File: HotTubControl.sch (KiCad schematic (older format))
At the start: 27 parts, among them J1 Wasser Vorlauf, J2 Wasser Rücklauf, J3 Massagepumpe, J4 Filterpumpe, J5 Füllstandsensor, J6 Conn_01x03, K1 JV-KT, Q1 BC337, Q2 BSS138

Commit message: neue 3d Elemente
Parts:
- B1: symbol LoraClient-eagle-import:WEMOS-D1-MINI -> HotTubControl-rescue:WEMOS-D1-MINI-LoraClient-eagle-import
- C2: symbol LoraClient-eagle-import:CPOL-EU085CS-1AR -> Device:CP
- K1: symbol LoraClient-eagle-import:JV-KT -> HotTubControl-rescue:JV-KT-LoraClient-eagle-import
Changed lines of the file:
@@
 $EndComp
 $Comp
-L LoraClient-eagle-import:JV-KT K1
+L HotTubControl-rescue:JV-KT-LoraClient-eagle-import K1
 U 1 1 61660A14
 P 3700 4950
@@
 	1950 3950 2000 3950
 $Comp
-L LoraClient-eagle-import:JV-KT K1
+L HotTubControl-rescue:JV-KT-LoraClient-eagle-import K1
 U 2 1 6166404C
 P 1750 3750
@@
 Connection ~ 1650 5300
 $Comp
-L LoraClient-eagle-import:WEMOS-D1-MINI B1
+L HotTubControl-rescue:WEMOS-D1-MINI-LoraClient-eagle-import B1
 U 1 1 616A05F9
 P 5750 3700
@@
 	9300 4750 8400 4750
 $Comp
-L LoraClient-eagle-import:CPOL-EU085CS-1AR C2
+L Device:CP C2
 U 1 1 61684BD0
 P 1800 5100

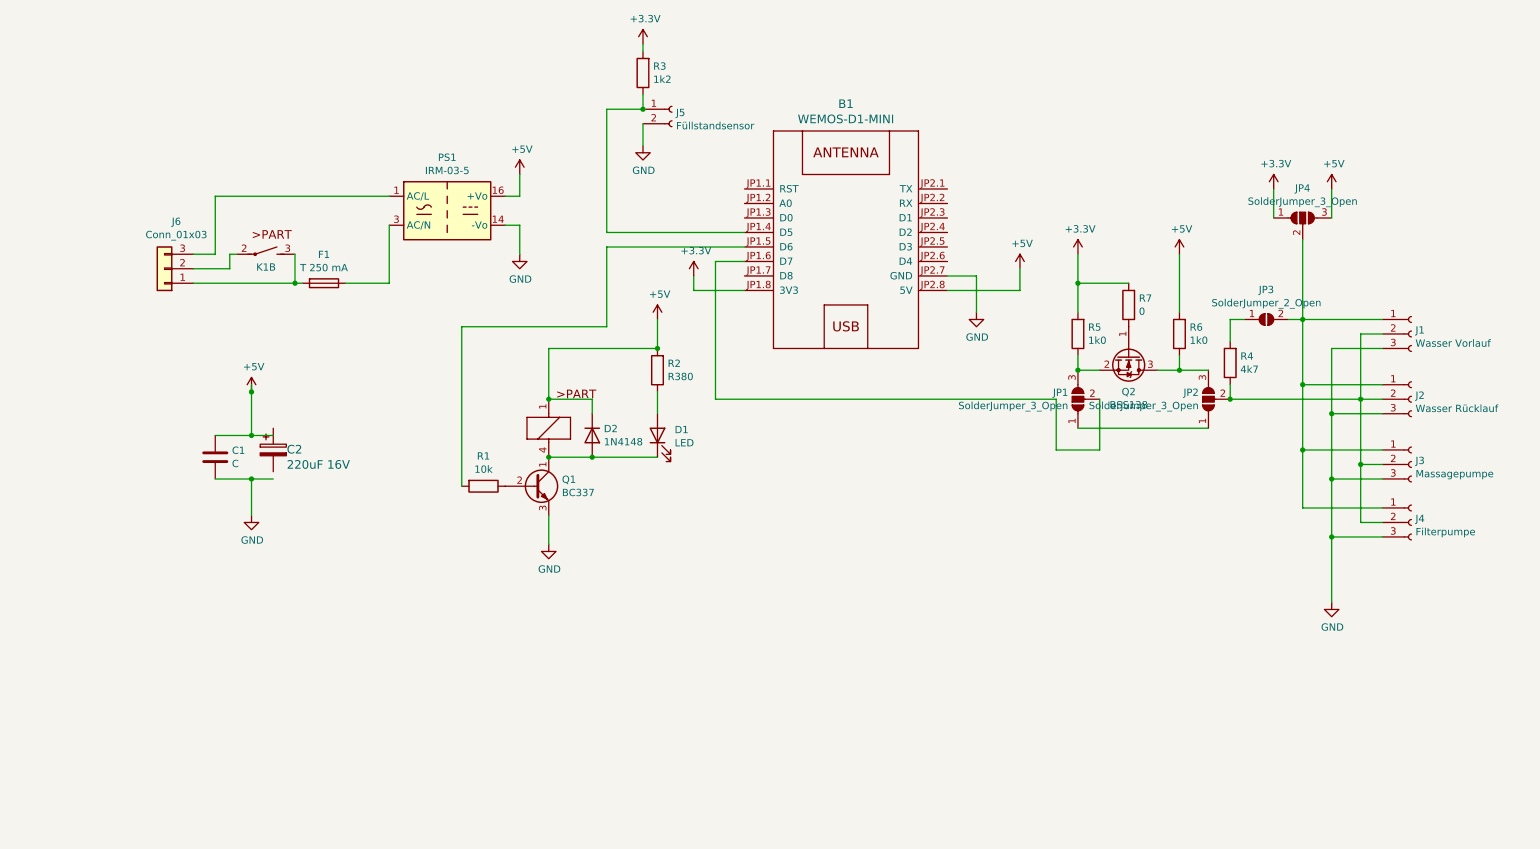
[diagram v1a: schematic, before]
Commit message: V2.0 added one channesl
Ein zweiter Relaiskanal zu Steuerung der  Massagepumpe wurde integriert
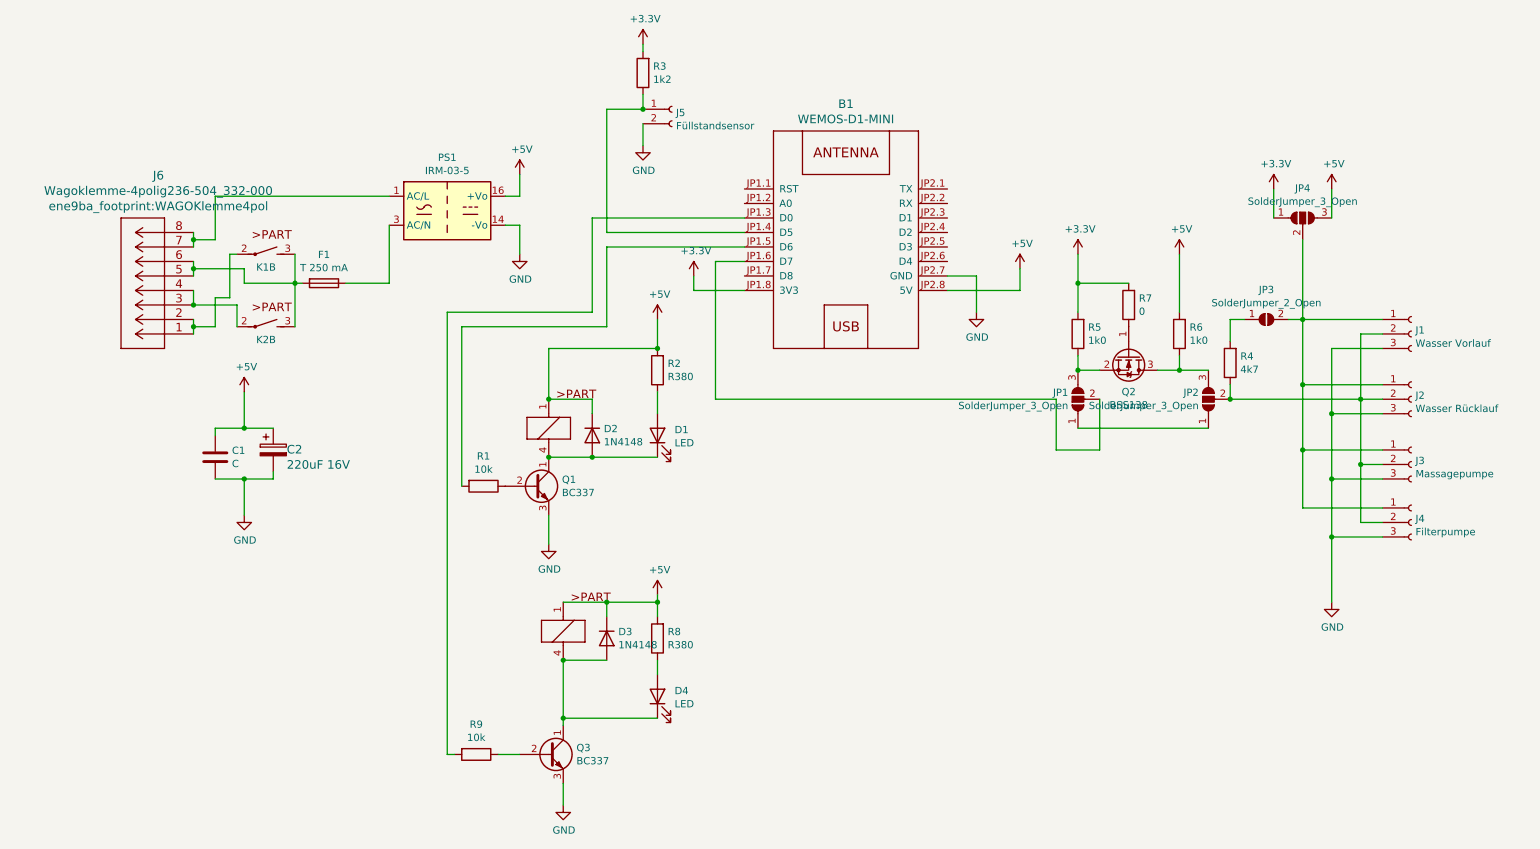
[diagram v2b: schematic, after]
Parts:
- removed J6: Conn_01x03, ene9ba_footprint:236-503, symbol Connector_Generic:Conn_01x03
- added D3: 1N4148, Diode_THT:D_DO-35_SOD27_P7.62mm_Horizontal, symbol Diode:1N4148
- added D4: LED, LED_THT:LED_D5.0mm, symbol Device:LED
- added J6: Wagoklemme-4polig236-504_332-000, ene9ba_footprint:WAGOKlemme4pol, symbol HotTubControl-rescue:Wagoklemme-4polig236-504_332-000-ene9ba_library
- added K2: JV-KT, SamacSys_Parts:JV24SKT, symbol HotTubControl-rescue:JV-KT-LoraClient-eagle-import
- added Q3: BC337, Package_TO_SOT_THT:TO-92_Inline, symbol Transistor_BJT:BC337
- added R8: R380, Resistor_THT:R_Axial_DIN0207_L6.3mm_D2.5mm_P15.24mm_Horizontal, symbol Device:R
- added R9: 10k, Resistor_THT:R_Axial_DIN0207_L6.3mm_D2.5mm_P15.24mm_Horizontal, symbol Device:R
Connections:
- wire segments 93 -> 125
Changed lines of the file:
@@
 L power:GND #PWR0104
 U 1 1 6169E8F8
-P 1650 5550
-F 0 "#PWR0104" H 1650 5300 50  0001 C CNN
-F 1 "GND" H 1655 5377 50  0000 C CNN
-F 2 "" H 1650 5550 50  0001 C CNN
-F 3 "" H 1650 5550 50  0001 C CNN
-	1    1650 5550
-	1    0    0    -1
-$EndComp
-Wire Wire Line
-	1400 5000 1650 5000
-Wire Wire Line
-	1650 5000 1650 4700
-Connection ~ 1650 5000
-Wire Wire Line
-	1650 5000 1800 5000
-Wire Wire Line
-	1650 5550 1650 5300
-Wire Wire Line
-	1400 5300 1650 5300
-Wire Wire Line
-	1650 5300 1800 5300
-Connection ~ 1650 5300
+P 1600 5550
+F 0 "#PWR0104" H 1600 5300 50  0001 C CNN
+F 1 "GND" H 1605 5377 50  0000 C CNN
+F 2 "" H 1600 5550 50  0001 C CNN
+F 3 "" H 1600 5550 50  0001 C CNN
+	1    1600 5550
+	1    0    0    -1
+$EndComp
 $Comp
 L HotTubControl-rescue:WEMOS-D1-MINI-LoraClient-eagle-import B1
@@
 L power:+5V #PWR0112
 U 1 1 61734FF9
-P 1650 4700
-F 0 "#PWR0112" H 1650 4550 50  0001 C CNN
-F 1 "+5V" H 1665 4873 50  0000 C CNN
-F 2 "" H 1650 4700 50  0001 C CNN
-F 3 "" H 1650 4700 50  0001 C CNN
-	1    1650 4700
-	1    0    0    -1
-$EndComp
-Connection ~ 1650 4700
-Wire Wire Line
-	1650 4700 1650 4650
+P 1600 4700
+F 0 "#PWR0112" H 1600 4550 50  0001 C CNN
+F 1 "+5V" H 1615 4873 50  0000 C CNN
+F 2 "" H 1600 4700 50  0001 C CNN
+F 3 "" H 1600 4700 50  0001 C CNN
+	1    1600 4700
+	1    0    0    -1
+$EndComp
 $Comp
 L power:+3.3V #PWR0113
@@
 	1    0    0    -1
 $EndComp
-$Comp
-L Connector_Generic:Conn_01x03 J6
-U 1 1 617860F2
-P 1050 3850
-F 0 "J6" H 968 3525 50  0000 C CNN
-F 1 "Conn_01x03" H 968 3616 50  0000 C CNN
-F 2 "ene9ba_footprint:236-503" H 1050 3850 50  0001 C CNN
-F 3 "~" H 1050 3850 50  0001 C CNN
-	1    1050 3850
-	-1   0    0    1
-$EndComp
-Wire Wire Line
-	1250 3950 1950 3950
 Connection ~ 1950 3950
 Wire Wire Line
 	1550 3750 1500 3750
-Wire Wire Line
-	1500 3750 1500 3850
-Wire Wire Line
-	1500 3850 1250 3850
-Wire Wire Line
-	1250 3750 1400 3750
-Wire Wire Line
-	1400 3750 1400 3350
 Wire Wire Line
 	1400 3350 2600 3350
@@
 Wire Wire Line
 	7350 3950 7350 4150
+$Comp
+L power:+5V #PWR0117
+U 1 1 618D82FF
+P 4450 6100
+F 0 "#PWR0117" H 4450 5950 50  0001 C CNN
+F 1 "+5V" H 4465 6273 50  0000 C CNN
+F 2 "" H 4450 6100 50  0001 C CNN
+F 3 "" H 4450 6100 50  0001 C CNN
+	1    4450 6100
+	1    0    0    -1
+$EndComp
+$Comp
+L Device:R R8
+U 1 1 618D957A
+P 4450 6400
+F 0 "R8" H 4380 6354 50  0000 R CNN
+F 1 "R380" H 4380 6445 50  0000 R CNN
+F 2 "Resistor_THT:R_Axial_DIN0207_L6.3mm_D2.5mm_P15.24mm_Horizontal" V 4380 6400 50  0001 C CNN
+F 3 "~" H 4450 6400 50  0001 C CNN
+	1    4450 6400
+	-1   0    0    1
+$EndComp
+$Comp
+L HotTubControl-rescue:JV-KT-LoraClient-eagle-import K2
+U 1 1 618DA08B
+P 3800 6350
+F 0 "K2" H 3800 6350 50  0001 C CNN
+F 1 "JV-KT" H 3850 6465 59  0001 L BNN
+F 2 "SamacSys_Parts:JV24SKT" H 3800 6350 50  0001 C CNN
+F 3 "" H 3800 6350 50  0001 C CNN
+	1    3800 6350
+	1    0    0    -1
+$EndComp
+$Comp
+L Diode:1N4148 D3
+U 1 1 618DD5D3
+P 4100 6400
+F 0 "D3" V 4054 6480 50  0000 L CNN
+F 1 "1N4148" V 4145 6480 50  0000 L CNN
+F 2 "Diode_THT:D_DO-35_SOD27_P7.62mm_Horizontal" H 4100 6225 50  0001 C CNN
+F 3 "https://assets.nexperia.com/documents/data-sheet/1N4148_1N4448.pdf" H 4100 6400 50  0001 C CNN
+	1    4100 6400
+	0    1    1    0
+$EndComp
+$Comp
+L Device:LED D4
+U 1 1 618DED1E
+P 4450 6800
+F 0 "D4" V 4489 6682 50  0000 R CNN
+F 1 "LED" V 4398 6682 50  0000 R CNN
+F 2 "LED_THT:LED_D5.0mm" H 4450 6800 50  0001 C CNN
+F 3 "~" H 4450 6800 50  0001 C CNN
+	1    4450 6800
+	0    -1   -1   0
+$EndComp
+$Comp
+L Transistor_BJT:BC337 Q3
+U 1 1 618DF9A8
+P 3700 7200
+F 0 "Q3" H 3891 7246 50  0000 L CNN
+F 1 "BC337" H 3891 7155 50  0000 L CNN
+F 2 "Package_TO_SOT_THT:TO-92_Inline" H 3900 7125 50  0001 L CIN
+F 3 "https://diotec.com/tl_files/diotec/files/pdf/datasheets/bc337.pdf" H 3700 7200 50  0001 L CNN
+	1    3700 7200
+	1    0    0    -1
+$EndComp
+$Comp
+L Device:R R9
+U 1 1 618E161A
+P 3200 7200
+F 0 "R9" V 2993 7200 50  0000 C CNN
+F 1 "10k" V 3084 7200 50  0000 C CNN
+F 2 "Resistor_THT:R_Axial_DIN0207_L6.3mm_D2.5mm_P15.24mm_Horizontal" V 3130 7200 50  0001 C CNN
+F 3 "~" H 3200 7200 50  0001 C CNN
+	1    3200 7200
+	0    1    1    0
+$EndComp
+$Comp
+L power:GND #PWR0118
+U 1 1 618E1F2A
+P 3800 7550
+F 0 "#PWR0118" H 3800 7300 50  0001 C CNN
+F 1 "GND" H 3805 7377 50  0000 C CNN
+F 2 "" H 3800 7550 50  0001 C CNN
+F 3 "" H 3800 7550 50  0001 C CNN
+	1    3800 7550
+	1    0    0    -1
+$EndComp
+Wire Wire Line
+	4450 6100 4450 6150
+Wire Wire Line
+	4450 6550 4450 6650
+Wire Wire Line
+	4450 6950 3800 6950
+Wire Wire Line
+	3800 6950 3800 7000
+Wire Wire Line
+	4100 6550 3800 6550
+Wire Wire Line
+	4100 6250 4100 6150
+Wire Wire Line
+	4100 6150 3800 6150
+Wire Wire Line
+	4100 6150 4450 6150
+Connection ~ 4100 6150
+Connection ~ 4450 6150
+Wire Wire Line
+	4450 6150 4450 6250
+Wire Wire Line
+	3800 6550 3800 6950
+Connection ~ 3800 6550
+Connection ~ 3800 6950
+Wire Wire Line
+	3500 7200 3350 7200
+Wire Wire Line
+	5050 3500 4000 3500
+Wire Wire Line
+	4000 3500 4000 4150
+Wire Wire Line
+	4000 4150 3000 4150
+Wire Wire Line
+	3000 4150 3000 7200
+Wire Wire Line
+	3000 7200 3050 7200
+$Comp
+L HotTubControl-rescue:JV-KT-LoraClient-eagle-import K2
+U 2 1 61907E3E
+P 1750 4250
+F 0 "K2" V 1840 4250 50  0000 C CNN
+F 1 "JV-KT" H 1800 4365 59  0001 L BNN
+F 2 "SamacSys_Parts:JV24SKT" H 1750 4250 50  0001 C CNN
+F 3 "" H 1750 4250 50  0001 C CNN
+	2    1750 4250
+	0    1    1    0
+$EndComp
+Wire Wire Line
+	1950 4250 1950 3950
+Wire Wire Line
+	3800 7400 3800 7550
+$Comp
+L HotTubControl-rescue:Wagoklemme-4polig236-504_332-000-ene9ba_library J6
+U 1 1 618FBF2D
+P 1250 4300
+F 0 "J6" H 1492 3207 60  0000 C CNN
+F 1 "Wagoklemme-4polig236-504_332-000" H 1492 3313 60  0000 C CNN
+F 2 "ene9ba_footprint:WAGOKlemme4pol" H 1492 3419 60  0000 C CNN
+F 3 "" H 1250 4300 60  0000 C CNN
+	1    1250 4300
+	-1   0    0    1
+$EndComp
+Wire Wire Line
+	1250 3700 1250 3650
+Wire Wire Line
+	1250 3800 1250 3850
+Wire Wire Line
+	1500 3750 1500 4050
+Wire Wire Line
+	1950 3950 1600 3950
+Wire Wire Line
+	1600 3950 1600 3850
+Wire Wire Line
+	1600 3850 1250 3850
+Connection ~ 1250 3850
+Wire Wire Line
+	1250 3850 1250 3900
+Wire Wire Line
+	1400 3350 1400 3650
+Wire Wire Line
+	1400 3650 1250 3650
+Connection ~ 1250 3650
+Wire Wire Line
+	1250 3650 1250 3600
+Wire Wire Line
+	1250 4200 1250 4250
+Wire Wire Line
+	1250 4000 1250 4100
+Wire Wire Line
+	1500 4050 1400 4050
+Wire Wire Line
+	1400 4050 1400 4250
+Wire Wire Line
+	1400 4250 1250 4250
+Connection ~ 1250 4250
+Wire Wire Line
+	1250 4250 1250 4300
+Wire Wire Line
+	1550 4250 1550 4100
+Wire Wire Line
+	1550 4100 1250 4100
+Connection ~ 1250 4100
+Wire Wire Line
+	1800 5300 1800 5250
+Wire Wire Line
+	1400 5300 1600 5300
+Wire Wire Line
+	1800 4950 1600 4950
+Wire Wire Line
+	1400 4950 1400 5000
+Wire Wire Line
+	1600 4700 1600 4950
+Connection ~ 1600 4950
+Wire Wire Line
+	1600 4950 1400 4950
+Wire Wire Line
+	1600 5550 1600 5300
+Connection ~ 1600 5300
+Wire Wire Line
+	1600 5300 1800 5300
 $EndSCHEMATC
